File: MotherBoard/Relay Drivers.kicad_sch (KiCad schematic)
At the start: 5 parts, among them Q701 NMOS, Q702 NPN

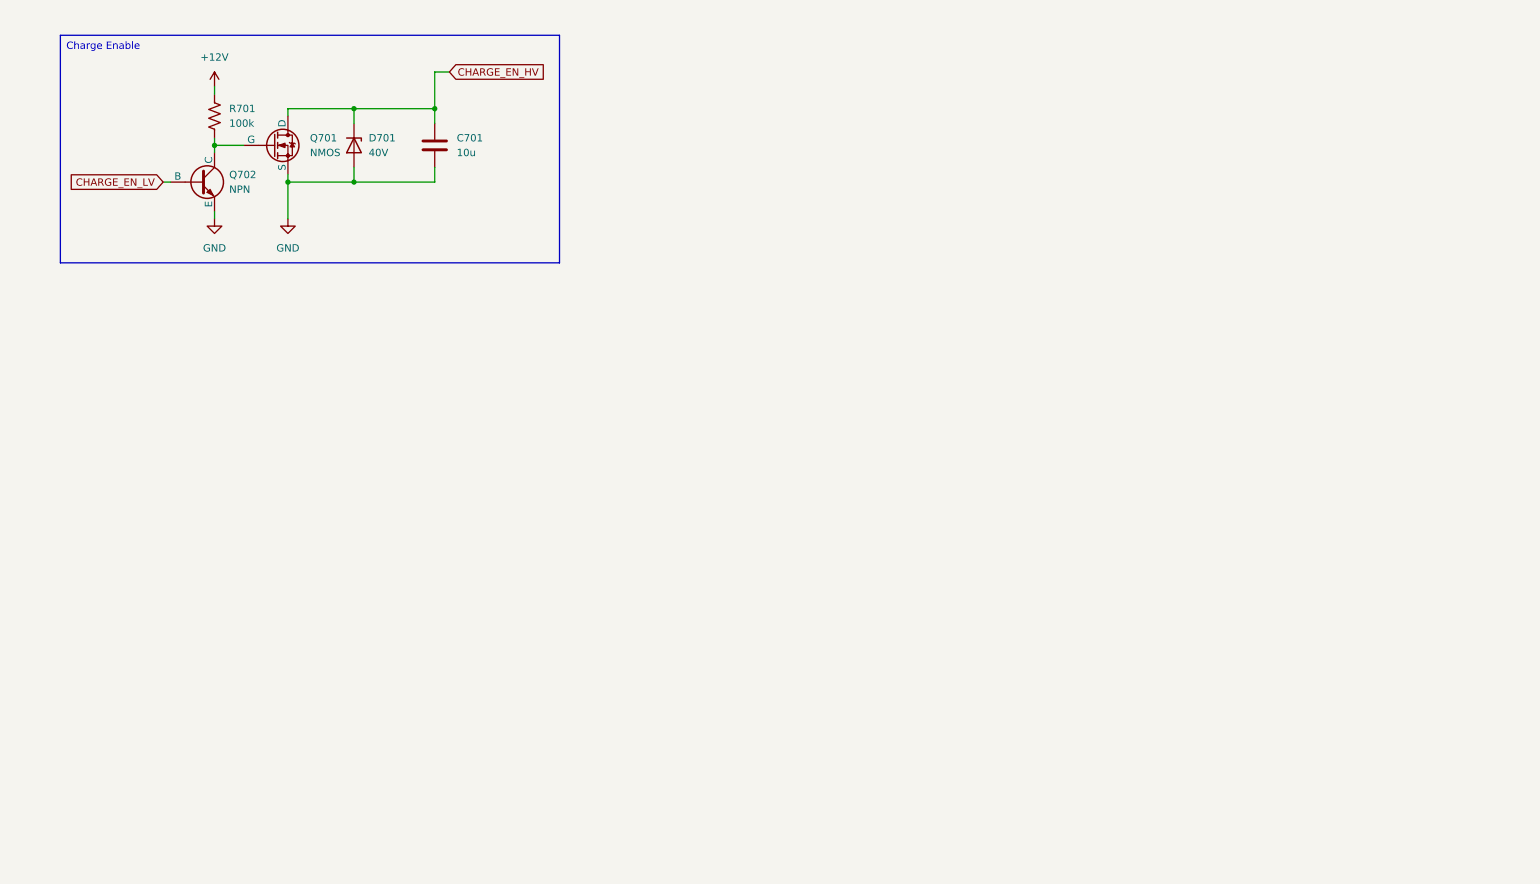
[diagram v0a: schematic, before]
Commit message: Revised all schematics + completed relay driver page
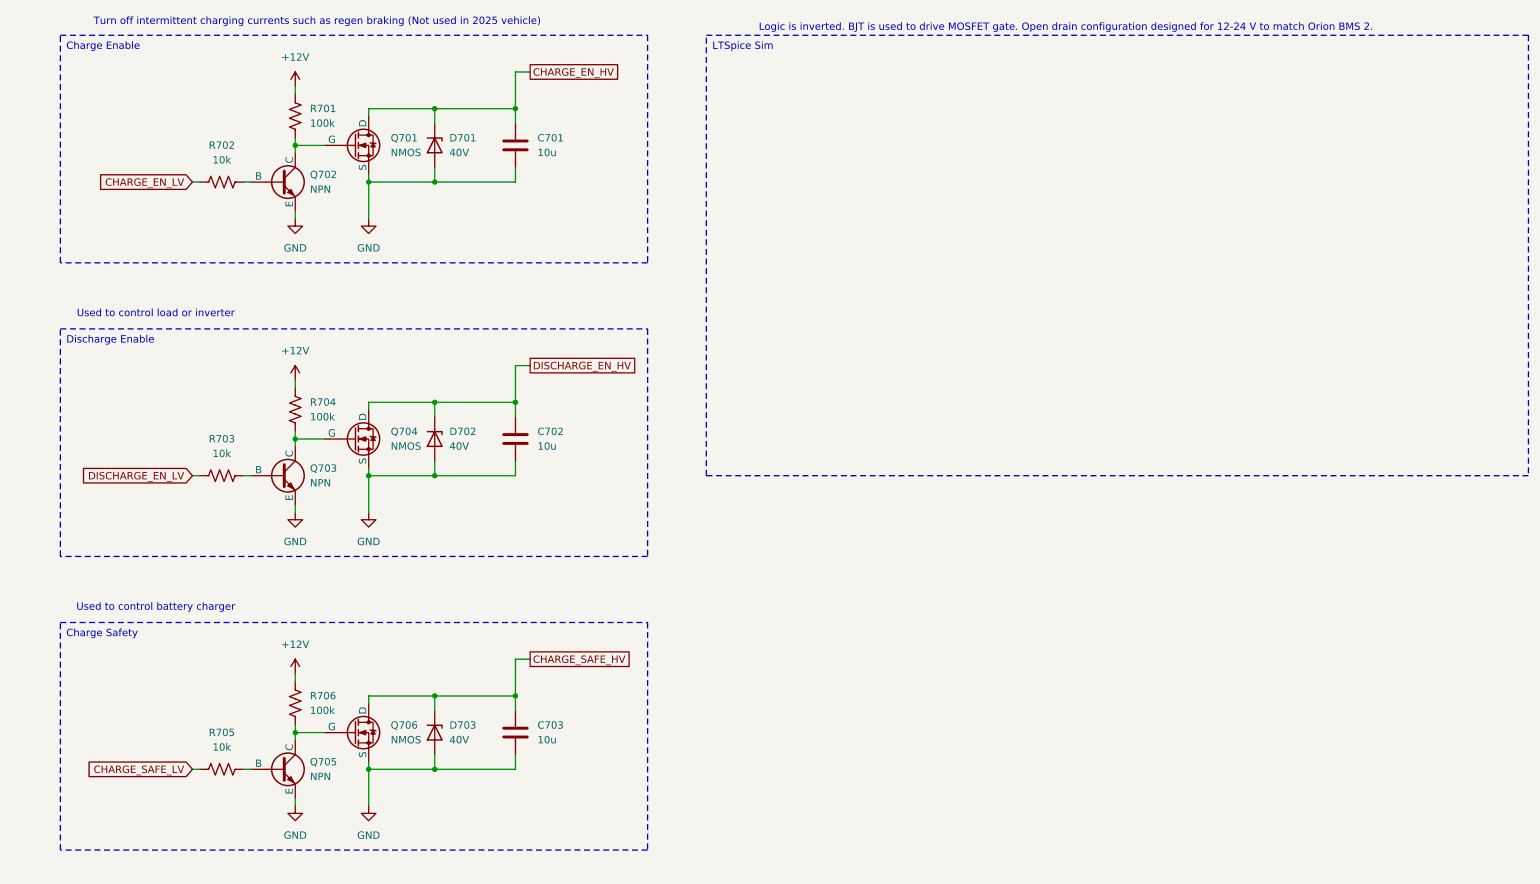
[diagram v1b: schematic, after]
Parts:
- added C702, C703: 10u, symbol Device:C
- added D702, D703: 40V, symbol Device:D_Zener
- added Q703, Q705: NPN, symbol Simulation_SPICE:NPN
- added Q704, Q706: NMOS, symbol Simulation_SPICE:NMOS
- added R702, R703, R705: 10k, symbol Device:R_US
- added R704, R706: 100k, symbol Device:R_US
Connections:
- net +12V: now also R704.1, R706.1
- net CHARGE_EN_LV: now also R702.1; no longer Q702.2 (B)
- net GND: now also C702.2, C703.2, D702.2 (A), D703.2 (A), Q703.3 (E), Q704.3 (S), Q705.3 (E), Q706.3 (S)
- new net: Q705.2 (B), R705.2
- new net: Q705.1 (C), Q706.2 (G), R706.2
- new net: Q703.1 (C), Q704.2 (G), R704.2
- new net: Q702.2 (B), R702.2
- new net: Q703.2 (B), R703.2
- new net CHARGE_SAFE_HV: C703.1, D703.1 (K), Q706.1 (D)
- new net CHARGE_SAFE_LV: R705.1
- new net DISCHARGE_EN_HV: C702.1, D702.1 (K), Q704.1 (D)
- new net DISCHARGE_EN_LV: R703.1
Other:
- note added: "Logic is inverted. BJT is used to drive MOSFET gate. Open drain configuration designed for 12-24 V to match Orion BMS 2."
- note added: "Turn off intermittent charging currents such as regen braking (Not used in 2025 vehicle)"
- note added: "Used to control battery charger"
- note added: "Used to control load or inverter"
- moved on the sheet: C701, D701, Q701, Q702, R701

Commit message: Fixed 3D model paths. Finished PSU ORing shcematic.
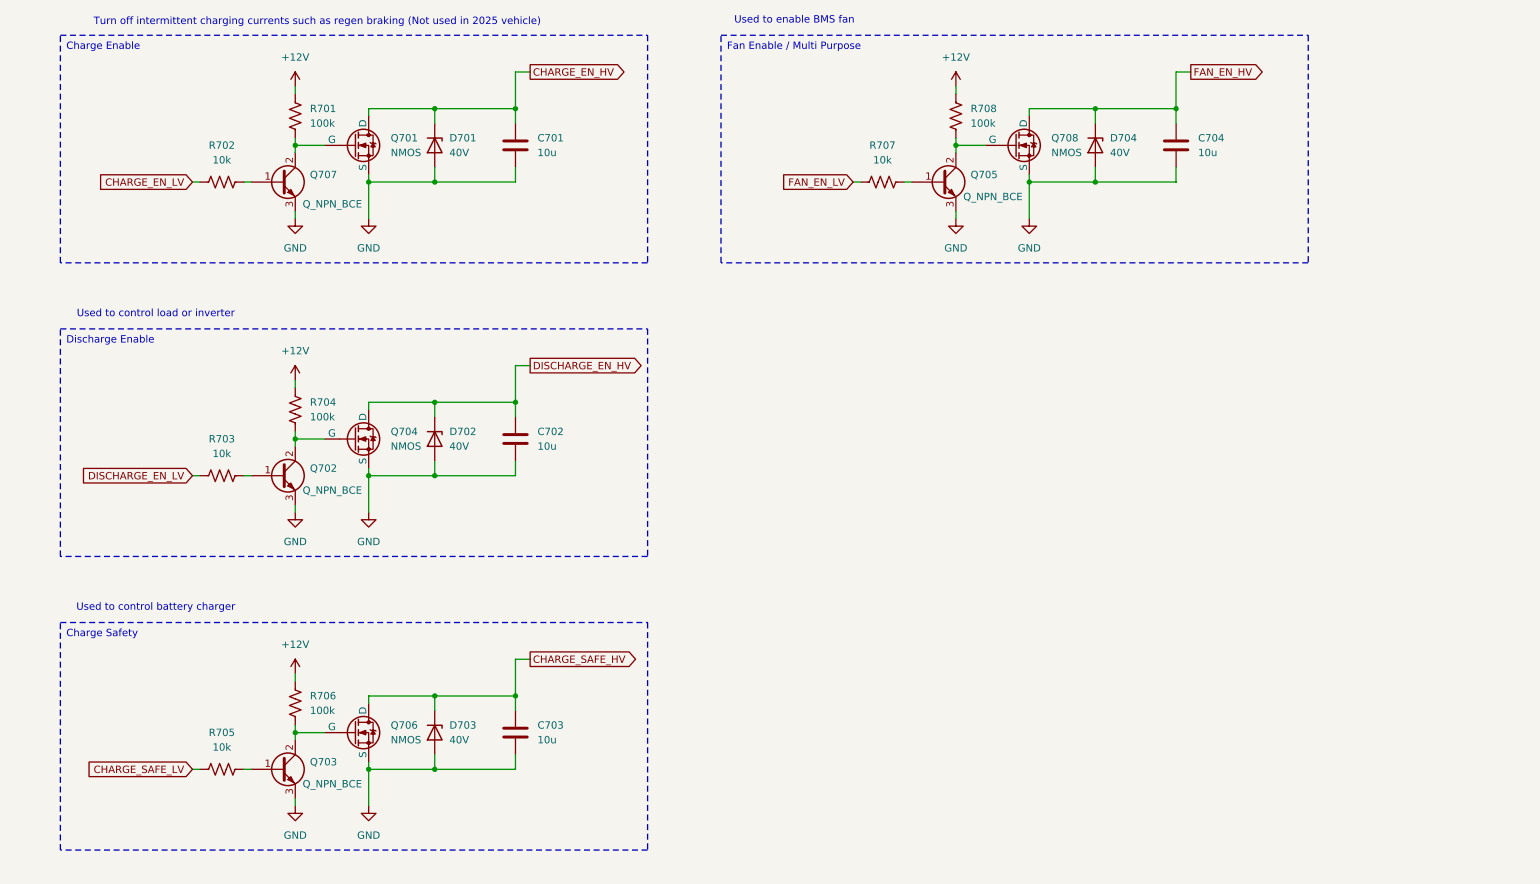
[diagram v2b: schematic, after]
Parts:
- removed Q702, Q703, Q705: NPN, symbol Simulation_SPICE:NPN
- added C704: 10u, symbol Device:C
- added D704: 40V, symbol Device:D_Zener
- added Q702, Q703, Q705, Q707: Q_NPN_BCE, symbol Device:Q_NPN_BCE
- added Q708: NMOS, symbol Simulation_SPICE:NMOS
- added R707: 10k, symbol Device:R_US
- added R708: 100k, symbol Device:R_US
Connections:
- net +12V: now also R708.1
- net GND: now also C704.2, D704.2 (A), Q702.3 (E), Q703.3 (E), Q705.3 (E), Q707.3 (E), Q708.3 (S)
- net at Q701.2 (G), R701.2: now also Q707.2 (C)
- net at R705.2: now also Q703.1 (B)
- net at Q706.2 (G), R706.2: now also Q703.2 (C)
- net at Q704.2 (G), R704.2: now also Q702.2 (C)
- net at R702.2: now also Q707.1 (B)
- net at R703.2: now also Q702.1 (B)
- new net: Q705.2 (C), Q708.2 (G), R708.2
- new net: Q705.1 (B), R707.2
- new net FAN_EN_HV: C704.1, D704.1 (K), Q708.1 (D)
- new net FAN_EN_LV: R707.1
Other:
- note added: "Used to enable BMS fan"
- note removed: "Logic is inverted. BJT is used to drive MOSFET gate. Open drain configuration designed for 12-24 V to match Orion BMS 2."

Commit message: Added more 3D models
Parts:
- C701, C702, C703, C704: footprint (none) -> Capacitor_SMD:C_0603_1608Metric
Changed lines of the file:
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@@
 			)
 		)
-		(property "Footprint" ""
+		(property "Footprint" "Capacitor_SMD:C_0603_1608Metric"
 			(at 219.4052 48.26 0)
 			(effects
@@
 			)
 		)
-		(property "Footprint" ""
+		(property "Footprint" "Capacitor_SMD:C_0603_1608Metric"
 			(at 105.1052 48.26 0)
 			(effects
@@
 			)
 		)
-		(property "Footprint" ""
+		(property "Footprint" "Capacitor_SMD:C_0603_1608Metric"
 			(at 105.1052 149.86 0)
 			(effects
@@
 			)
 		)
-		(property "Footprint" ""
+		(property "Footprint" "Capacitor_SMD:C_0603_1608Metric"
 			(at 105.1052 99.06 0)
 			(effects

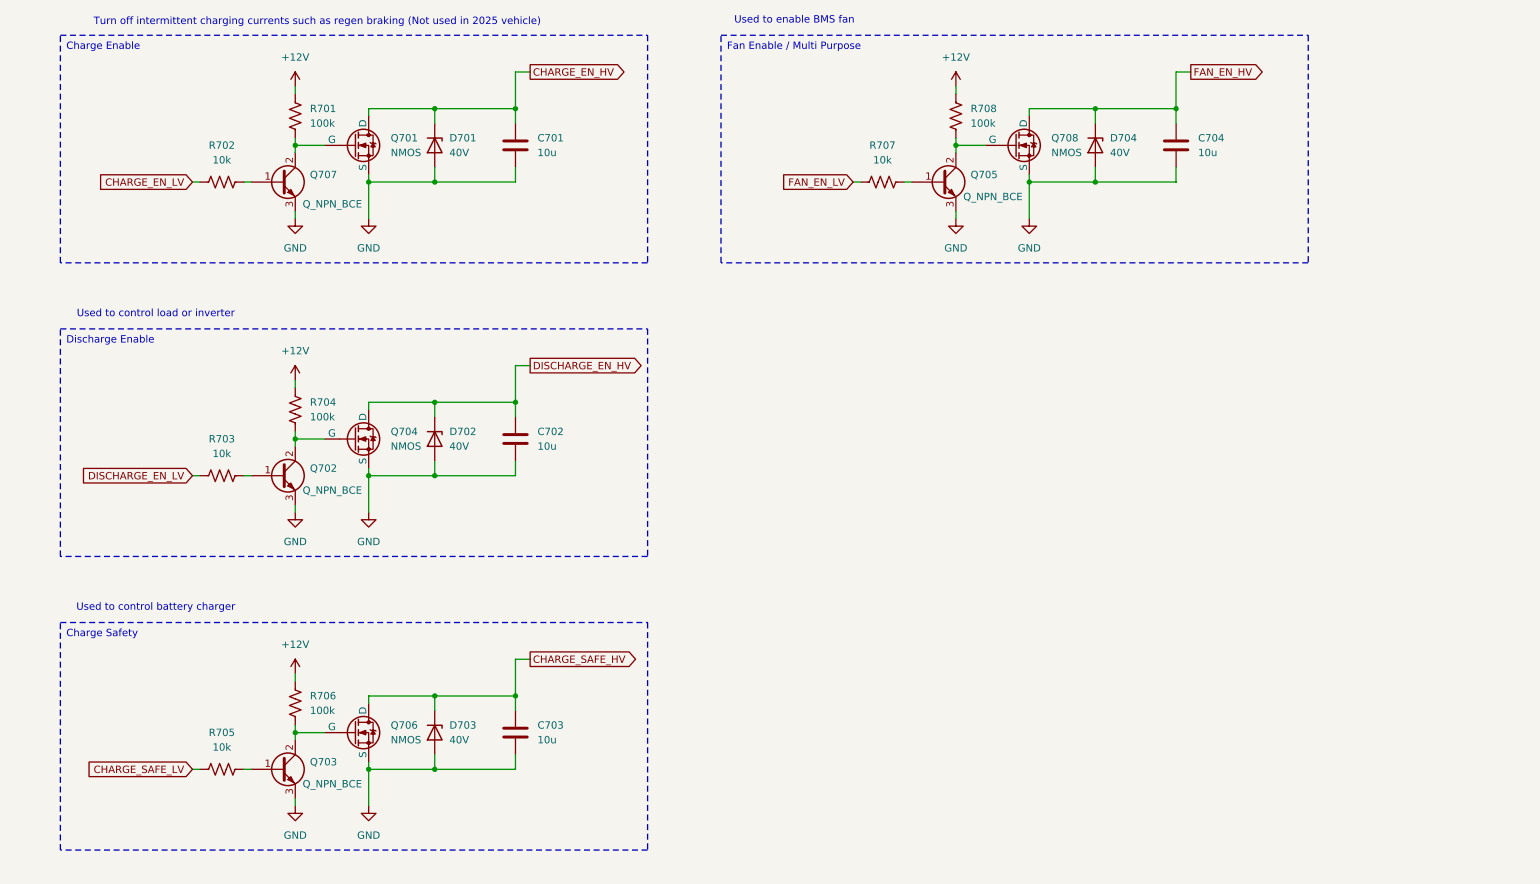
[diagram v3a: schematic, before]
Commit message: Fixed relative paths + 90% footprints done + organized PCB for layout + found JLC part #s for manufacturing
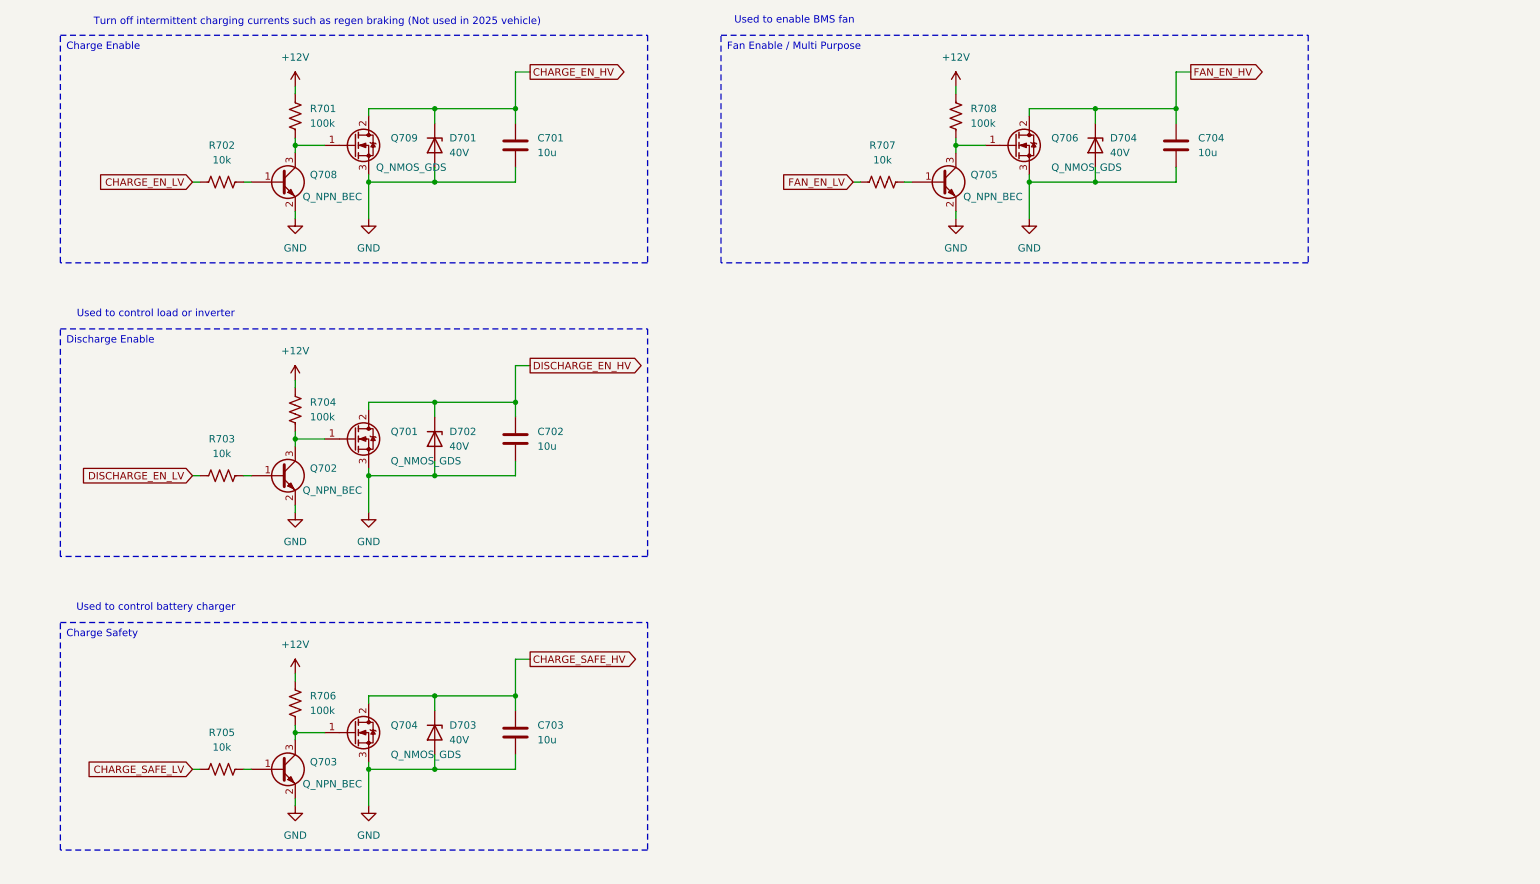
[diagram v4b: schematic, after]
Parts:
- removed Q701, Q704, Q706, Q708: NMOS, symbol Simulation_SPICE:NMOS
- removed Q702, Q703, Q705, Q707: Q_NPN_BCE, symbol Device:Q_NPN_BCE
- added Q701, Q704, Q706, Q709: Q_NMOS_GDS, Package_TO_SOT_SMD:TO-263-2, symbol Device:Q_NMOS_GDS
- added Q702, Q703, Q705, Q708: Q_NPN_BEC, Package_TO_SOT_SMD:SOT-23, symbol Device:Q_NPN_BEC
- D701, D702, D703, D704: footprint (none) -> Diode_SMD:D_SOD-123; Manufacturer_Part_Number (none) -> BZT52C30
- R701, R702, R703, R704, R705, R706, R707, R708: footprint (none) -> Resistor_SMD:R_0402_1005Metric
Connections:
- net CHARGE_EN_HV: now also Q709.2 (D)
- net CHARGE_SAFE_HV: now also Q704.2 (D)
- net DISCHARGE_EN_HV: now also Q701.2 (D)
- net FAN_EN_HV: now also Q706.2 (D)
- net GND: now also Q701.3 (S), Q702.2 (E), Q703.2 (E), Q704.3 (S), Q705.2 (E), Q706.3 (S), Q708.2 (E), Q709.3 (S)
- net at R705.2: now also Q703.1 (B)
- net at R706.2: now also Q703.3 (C), Q704.1 (G)
- net at R701.2: now also Q708.3 (C), Q709.1 (G)
- net at R702.2: now also Q708.1 (B)
- net at R708.2: now also Q705.3 (C), Q706.1 (G)
- net at R707.2: now also Q705.1 (B)
- net at R703.2: now also Q702.1 (B)
- net at R704.2: now also Q701.1 (G), Q702.3 (C)

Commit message: Completed BOM except inductors
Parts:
- C701, C702, C703, C704: footprint Capacitor_SMD:C_0603_1608Metric -> Capacitor_SMD:C_1206_3216Metric; Manufacturer_Part_Number (none) -> CL31A106KBHNNNE
- R701, R704, R706, R708: Manufacturer_Part_Number (none) -> 0402WGF1003TCE
- R702, R703, R705, R707: Manufacturer_Part_Number (none) -> 0402WGF1001TCE
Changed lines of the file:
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@@
 			)
 		)
-		(property "Footprint" "Capacitor_SMD:C_0603_1608Metric"
+		(property "Footprint" "Capacitor_SMD:C_1206_3216Metric"
 			(at 219.4052 48.26 0)
 			(effects
@@
 		)
 		(property "Sim.Type" ""
+			(at 218.44 44.45 0)
+			(effects
+				(font
+					(size 1.27 1.27)
+				)
+				(hide yes)
+			)
+		)
+		(property "Manufacturer_Part_Number" "CL31A106KBHNNNE"
 			(at 218.44 44.45 0)
 			(effects
@@
 			)
 		)
+		(property "Manufacturer_Part_Number" "0402WGF1003TCE"
+			(at 180.34 39.37 0)
+			(effects
+				(font
+					(size 1.27 1.27)
+				)
+				(hide yes)
+			)
+		)
 		(pin "2"
 		)
@@
 			)
 		)
+		(property "Manufacturer_Part_Number" "0402WGF1001TCE"
+			(at 53.34 152.4 0)
+			(effects
+				(font
+					(size 1.27 1.27)
+				)
+				(hide yes)
+			)
+		)
 		(pin "2"
 		)
@@
 			)
 		)
+		(property "Manufacturer_Part_Number" "0402WGF1001TCE"
+			(at 167.64 50.8 0)
+			(effects
+				(font
+					(size 1.27 1.27)
+				)
+				(hide yes)
+			)
+		)
 		(pin "2"
 		)
@@
 			)
 		)
-		(property "Footprint" "Capacitor_SMD:C_0603_1608Metric"
+		(property "Footprint" "Capacitor_SMD:C_1206_3216Metric"
 			(at 105.1052 48.26 0)
 			(effects
@@
 		)
 		(property "Sim.Type" ""
+			(at 104.14 44.45 0)
+			(effects
+				(font
+					(size 1.27 1.27)
+				)
+				(hide yes)
+			)
+		)
+		(property "Manufacturer_Part_Number" "CL31A106KBHNNNE"
 			(at 104.14 44.45 0)
 			(effects
@@
 			)
 		)
+		(property "Manufacturer_Part_Number" "0402WGF1003TCE"
+			(at 66.04 39.37 0)
+			(effects
+				(font
+					(size 1.27 1.27)
+				)
+				(hide yes)
+			)
+		)
 		(pin "2"
 		)
@@
 			)
 		)
+		(property "Manufacturer_Part_Number" "0402WGF1003TCE"
+			(at 66.04 90.17 0)
+			(effects
+				(font
+					(size 1.27 1.27)
+				)
+				(hide yes)
+			)
+		)
 		(pin "2"
 		)
@@
 			)
 		)
+		(property "Manufacturer_Part_Number" "0402WGF1001TCE"
+			(at 53.34 50.8 0)
+			(effects
+				(font
+					(size 1.27 1.27)
+				)
+				(hide yes)
+			)
+		)
 		(pin "2"
 		)
@@
 			)
 		)
+		(property "Manufacturer_Part_Number" "0402WGF1001TCE"
+			(at 53.34 101.6 0)
+			(effects
+				(font
+					(size 1.27 1.27)
+				)
+				(hide yes)
+			)
+		)
 		(pin "2"
 		)
@@
 			)
 		)
+		(property "Manufacturer_Part_Number" "0402WGF1003TCE"
+			(at 66.04 140.97 0)
+			(effects
+				(font
+					(size 1.27 1.27)
+				)
+				(hide yes)
+			)
+		)
 		(pin "2"
 		)
@@
 			)
 		)
-		(property "Footprint" "Capacitor_SMD:C_0603_1608Metric"
+		(property "Footprint" "Capacitor_SMD:C_1206_3216Metric"
 			(at 105.1052 149.86 0)
 			(effects
@@
 		)
 		(property "Sim.Type" ""
+			(at 104.14 146.05 0)
+			(effects
+				(font
+					(size 1.27 1.27)
+				)
+				(hide yes)
+			)
+		)
+		(property "Manufacturer_Part_Number" "CL31A106KBHNNNE"
 			(at 104.14 146.05 0)
 			(effects
@@
 			)
 		)
-		(property "Footprint" "Capacitor_SMD:C_0603_1608Metric"
+		(property "Footprint" "Capacitor_SMD:C_1206_3216Metric"
 			(at 105.1052 99.06 0)
 			(effects
@@
 			(at 104.14 95.25 0)
 			(effects
+				(font
+					(size 1.27 1.27)
+				)
+				(hide yes)
+			)
+		)
+		(property "Manufacturer_Part_Number" "CL31A106KBHNNNE"
+			(at 104.14 95.25 0)
+			(effects
